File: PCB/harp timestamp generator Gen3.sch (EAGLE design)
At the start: 143 parts, among them IC1 MCP73831T-2ATI/OT, IC10 SN74LVC1G125DBVT, IC11 TLV70033DDCR, IC12 SI8621BC-B-IS, IC13 SI8621BC-B-IS, IC14 SI8621BC-B-IS, IC15 SI8621BC-B-IS, IC16 SI8621BC-B-IS, IC17 SI8621BC-B-IS, IC18 SN74LVC1G125DBVT, IC19 SN74LVC1G125DBVT, IC2 USBLC6-2SC6, IC3 FT232RL, IC4 ICL7673CBAZA-T, IC5 TLV70033DDCR, IC6 ATXMEGA16A4U-AU, IC7 M74VHC1GT126DF1G, IC8 M74VHC1GT126DF1G, IC9 M74VHC1GT126DF1G, Q1 RTU002P02T106, Q2 BC817-40W, Q3 BC817-40LT1SMD, Q4 DMG1012UW, Q5 DMP2035U-7, T1 BC850, T10 BC850, T2 BC850, T3 BC850, T4 BC850, T5 BC850, T6 BC850, T7 BC850, T8 BC850, T9 BC850, X1 B2B-PH-K-S(LF)(SN)

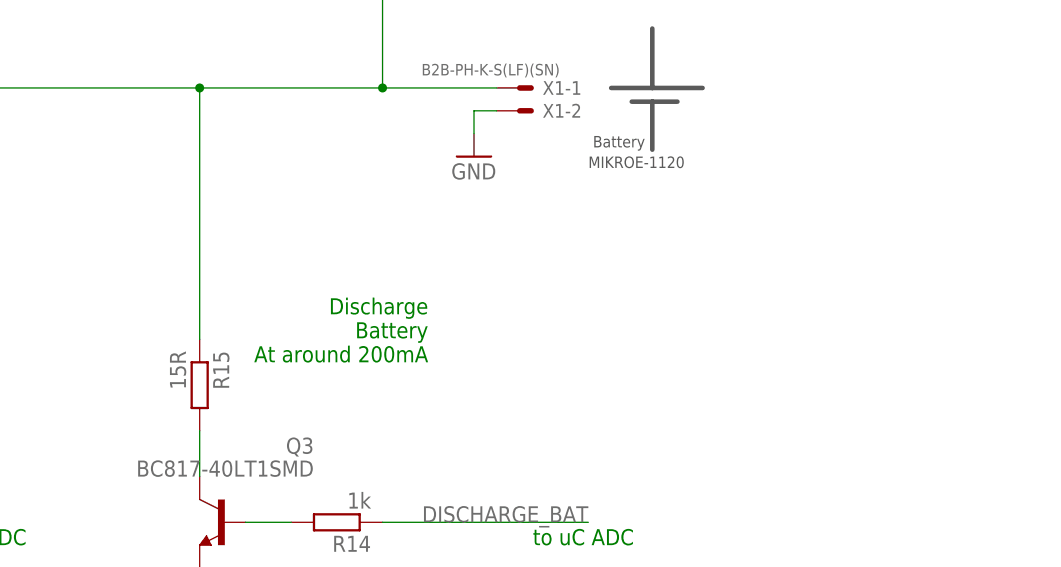
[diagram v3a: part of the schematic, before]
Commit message: Decreased discharge current by ~60 mA to ~175 mA in average.
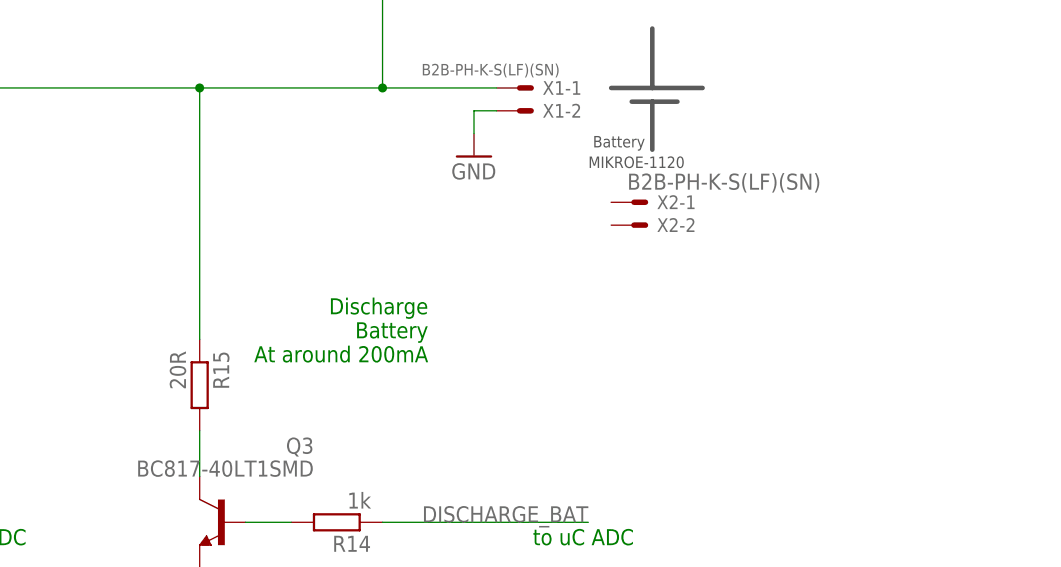
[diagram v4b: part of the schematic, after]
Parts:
- added X2: B2B-PH-K-S(LF)(SN), harp timestamp generator:JST-XH-02-PIN-ROUND-PAD
- R15: value 15R -> 20R
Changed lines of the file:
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@@
 <grid distance="100" unitdist="mil" unit="mil" style="lines" multiple="1" display="no" altdistance="0.01" altunitdist="inch" altunit="inch"/>
 <layers>
-<layer number="1" name="Top" color="4" fill="1" visible="no" active="no"/>
-<layer number="2" name="Route2" color="30" fill="1" visible="no" active="no"/>
-<layer number="3" name="Route3" color="4" fill="3" visible="no" active="no"/>
-<layer number="4" name="Route4" color="1" fill="4" visible="no" active="no"/>
-<layer number="5" name="Route5" color="4" fill="4" visible="no" active="no"/>
-<layer number="6" name="Route6" color="1" fill="8" visible="no" active="no"/>
-<layer number="7" name="Route7" color="4" fill="8" visible="no" active="no"/>
-<layer number="8" name="Route8" color="1" fill="2" visible="no" active="no"/>
-<layer number="9" name="Route9" color="4" fill="2" visible="no" active="no"/>
-<layer number="10" name="Route10" color="1" fill="7" visible="no" active="no"/>
-<layer number="11" name="Route11" color="4" fill="7" visible="no" active="no"/>
-<layer number="12" name="Route12" color="1" fill="5" visible="no" active="no"/>
-<layer number="13" name="Route13" color="4" fill="5" visible="no" active="no"/>
-<layer number="14" name="Route14" color="1" fill="6" visible="no" active="no"/>
-<layer number="15" name="Route15" color="16" fill="1" visible="no" active="no"/>
-<layer number="16" name="Bottom" color="1" fill="1" visible="no" active="no"/>
-<layer number="17" name="Pads" color="2" fill="1" visible="no" active="no"/>
-<layer number="18" name="Vias" color="2" fill="1" visible="no" active="no"/>
-<layer number="19" name="Unrouted" color="6" fill="1" visible="no" active="no"/>
-<layer number="20" name="Dimension" color="15" fill="1" visible="no" active="no"/>
-<layer number="21" name="tPlace" color="7" fill="1" visible="no" active="no"/>
-<layer number="22" name="bPlace" color="7" fill="1" visible="no" active="no"/>
-<layer number="23" name="tOrigins" color="15" fill="1" visible="no" active="no"/>
-<layer number="24" name="bOrigins" color="15" fill="1" visible="no" active="no"/>
-<layer number="25" name="tNames" color="7" fill="1" visible="no" active="no"/>
-<layer number="26" name="bNames" color="7" fill="1" visible="no" active="no"/>
-<layer number="27" name="tValues" color="7" fill="1" visible="no" active="no"/>
-<layer number="28" name="bValues" color="7" fill="1" visible="no" active="no"/>
+<layer number="1" name="Top" color="4" fill="1" visible="yes" active="no"/>
+<layer number="2" name="Route2" color="30" fill="1" visible="yes" active="no"/>
+<layer number="3" name="Route3" color="4" fill="3" visible="yes" active="no"/>
+<layer number="4" name="Route4" color="1" fill="4" visible="yes" active="no"/>
+<layer number="5" name="Route5" color="4" fill="4" visible="yes" active="no"/>
+<layer number="6" name="Route6" color="1" fill="8" visible="yes" active="no"/>
+<layer number="7" name="Route7" color="4" fill="8" visible="yes" active="no"/>
+<layer number="8" name="Route8" color="1" fill="2" visible="yes" active="no"/>
+<layer number="9" name="Route9" color="4" fill="2" visible="yes" active="no"/>
+<layer number="10" name="Route10" color="1" fill="7" visible="yes" active="no"/>
+<layer number="11" name="Route11" color="4" fill="7" visible="yes" active="no"/>
+<layer number="12" name="Route12" color="1" fill="5" visible="yes" active="no"/>
+<layer number="13" name="Route13" color="4" fill="5" visible="yes" active="no"/>
+<layer number="14" name="Route14" color="1" fill="6" visible="yes" active="no"/>
+<layer number="15" name="Route15" color="16" fill="1" visible="yes" active="no"/>
+<layer number="16" name="Bottom" color="1" fill="1" visible="yes" active="no"/>
+<layer number="17" name="Pads" color="2" fill="1" visible="yes" active="no"/>
+<layer number="18" name="Vias" color="2" fill="1" visible="yes" active="no"/>
+<layer number="19" name="Unrouted" color="6" fill="1" visible="yes" active="no"/>
+<layer number="20" name="Dimension" color="15" fill="1" visible="yes" active="no"/>
+<layer number="21" name="tPlace" color="7" fill="1" visible="yes" active="no"/>
+<layer number="22" name="bPlace" color="7" fill="1" visible="yes" active="no"/>
+<layer number="23" name="tOrigins" color="15" fill="1" visible="yes" active="no"/>
+<layer number="24" name="bOrigins" color="15" fill="1" visible="yes" active="no"/>
+<layer number="25" name="tNames" color="7" fill="1" visible="yes" active="no"/>
+<layer number="26" name="bNames" color="7" fill="1" visible="yes" active="no"/>
+<layer number="27" name="tValues" color="7" fill="1" visible="yes" active="no"/>
+<layer number="28" name="bValues" color="7" fill="1" visible="yes" active="no"/>
 <layer number="29" name="tStop" color="7" fill="3" visible="no" active="no"/>
 <layer number="30" name="bStop" color="7" fill="6" visible="no" active="no"/>
@@
 <layer number="35" name="tGlue" color="7" fill="4" visible="no" active="no"/>
 <layer number="36" name="bGlue" color="7" fill="5" visible="no" active="no"/>
-<layer number="37" name="tTest" color="7" fill="1" visible="no" active="no"/>
-<layer number="38" name="bTest" color="7" fill="1" visible="no" active="no"/>
+<layer number="37" name="tTest" color="7" fill="1" visible="yes" active="no"/>
+<layer number="38" name="bTest" color="7" fill="1" visible="yes" active="no"/>
 <layer number="39" name="tKeepout" color="4" fill="11" visible="no" active="no"/>
 <layer number="40" name="bKeepout" color="1" fill="11" visible="no" active="no"/>
@@
 <layer number="44" name="Drills" color="7" fill="1" visible="no" active="no"/>
 <layer number="45" name="Holes" color="7" fill="1" visible="no" active="no"/>
-<layer number="46" name="Milling" color="3" fill="1" visible="no" active="no"/>
-<layer number="47" name="Measures" color="7" fill="1" visible="no" active="no"/>
-<layer number="48" name="Document" color="7" fill="1" visible="no" active="no"/>
-<layer number="49" name="Reference" color="7" fill="1" visible="no" active="no"/>
-<layer number="50" name="dxf" color="7" fill="1" visible="no" active="no"/>
-<layer number="51" name="tDocu" color="7" fill="1" visible="no" active="no"/>
-<layer number="52" name="bDocu" color="7" fill="1" visible="no" active="no"/>
-<layer number="53" name="tGND_GNDA" color="7" fill="9" visible="no" active="no"/>
-<layer number="54" name="bGND_GNDA" color="1" fill="9" visible="no" active="no"/>
-<layer number="56" name="wert" color="7" fill="1" visible="no" active="no"/>
-<layer number="57" name="tCAD" color="7" fill="1" visible="no" active="no"/>
-<layer number="59" name="tCarbon" color="7" fill="1" visible="no" active="no"/>
-<layer number="60" name="bCarbon" color="7" fill="1" visible="no" active="no"/>
+<layer number="46" name="Milling" color="3" fill="1" visible="yes" active="no"/>
+<layer number="47" name="Measures" color="7" fill="1" visible="yes" active="no"/>
+<layer number="48" name="Document" color="7" fill="1" visible="yes" active="no"/>
+<layer number="49" name="Reference" color="7" fill="1" visible="yes" active="no"/>
+<layer number="50" name="dxf" color="7" fill="1" visible="yes" active="no"/>
+<layer number="51" name="tDocu" color="7" fill="1" visible="yes" active="no"/>
+<layer number="52" name="bDocu" color="7" fill="1" visible="yes" active="no"/>
+<layer number="53" name="tGND_GNDA" color="7" fill="9" visible="yes" active="no"/>
+<layer number="54" name="bGND_GNDA" color="1" fill="9" visible="yes" active="no"/>
+<layer number="56" name="wert" color="7" fill="1" visible="yes" active="no"/>
+<layer number="57" name="tCAD" color="7" fill="1" visible="yes" active="no"/>
+<layer number="59" name="tCarbon" color="7" fill="1" visible="yes" active="no"/>
+<layer number="60" name="bCarbon" color="7" fill="1" visible="yes" active="no"/>
 <layer number="88" name="SimResults" color="9" fill="1" visible="no" active="yes"/>
 <layer number="89" name="SimProbes" color="9" fill="1" visible="no" active="yes"/>
@@
 <attribute name="MPN" value="CRCW040210K0FKEDC"/>
 </part>
-<part name="R15" library="rcl" deviceset="R-EU_" device="R2512" value="15R">
+<part name="R15" library="rcl" deviceset="R-EU_" device="R2512" value="20R">
 <attribute name="DIGKEYPN" value="541-2662-1-ND"/>
 <attribute name="MPN" value="RCP2512W25R0GEB"/>
@@
 <part name="GND123" library="supply1" deviceset="GND" device=""/>
 <part name="VDD4" library="supply1" library_urn="urn:adsk.eagle:library:371" deviceset="VDD" device="" value="+3V3_u"/>
+<part name="X2" library="harp timestamp generator" deviceset="JST-XH-02-PIN" device="-ROUND-PAD" value="B2B-PH-K-S(LF)(SN)">
+<attribute name="DIGKEYPN" value="455-1704-ND"/>
+<attribute name="MPN" value="B2B-PH-K-S(LF)(SN)"/>
+</part>
 </parts>
 <sheets>
@@
 <attribute name="VALUE" x="741.68" y="487.68" size="1.778" layer="96" rot="R90"/>
 </instance>
+<instance part="X2" gate="-1" x="353.06" y="434.34" smashed="yes">
+<attribute name="NAME" x="355.6" y="433.578" size="1.524" layer="95"/>
+<attribute name="VALUE" x="352.298" y="435.737" size="1.778" layer="96"/>
+</instance>
+<instance part="X2" gate="-2" x="353.06" y="431.8" smashed="yes">
+<attribute name="NAME" x="355.6" y="431.038" size="1.524" layer="95"/>
+<attribute name="MPN" x="353.06" y="431.8" size="1.778" layer="96" display="off"/>
+<attribute name="DIGKEYPN" x="353.06" y="431.8" size="1.778" layer="96" display="off"/>
+<attribute name="MPN" x="353.06" y="431.8" size="1.778" layer="96" display="off"/>
+<attribute name="DIGKEYPN" x="353.06" y="431.8" size="1.778" layer="96" display="off"/>
+</instance>
 </instances>

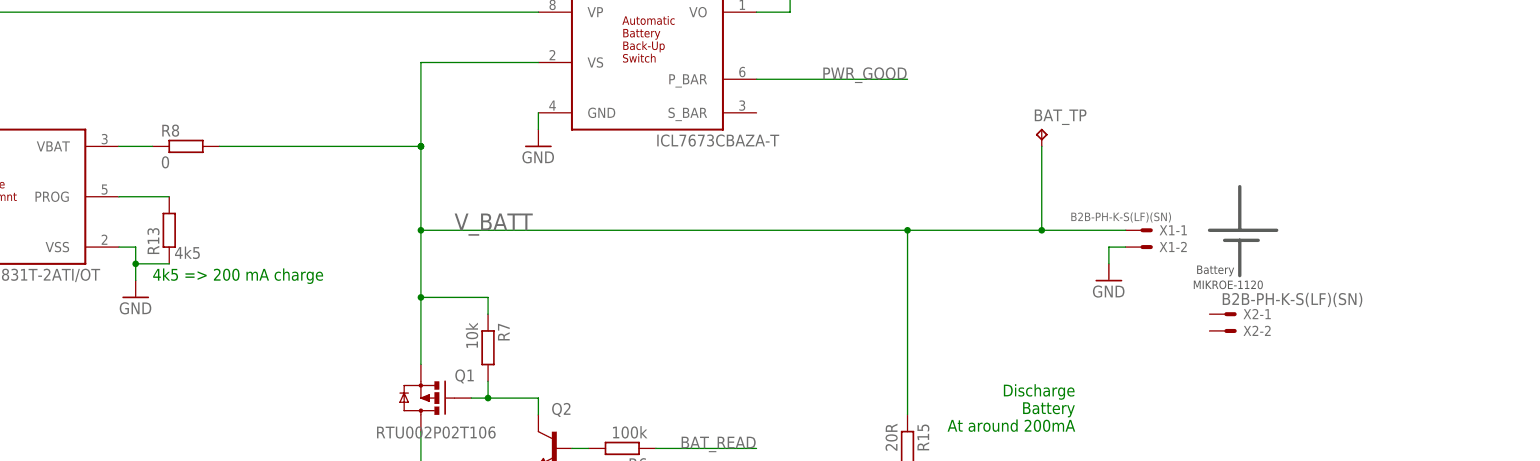
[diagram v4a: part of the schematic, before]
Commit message: Changed battery connection to a new location and added an ON/OFF button.
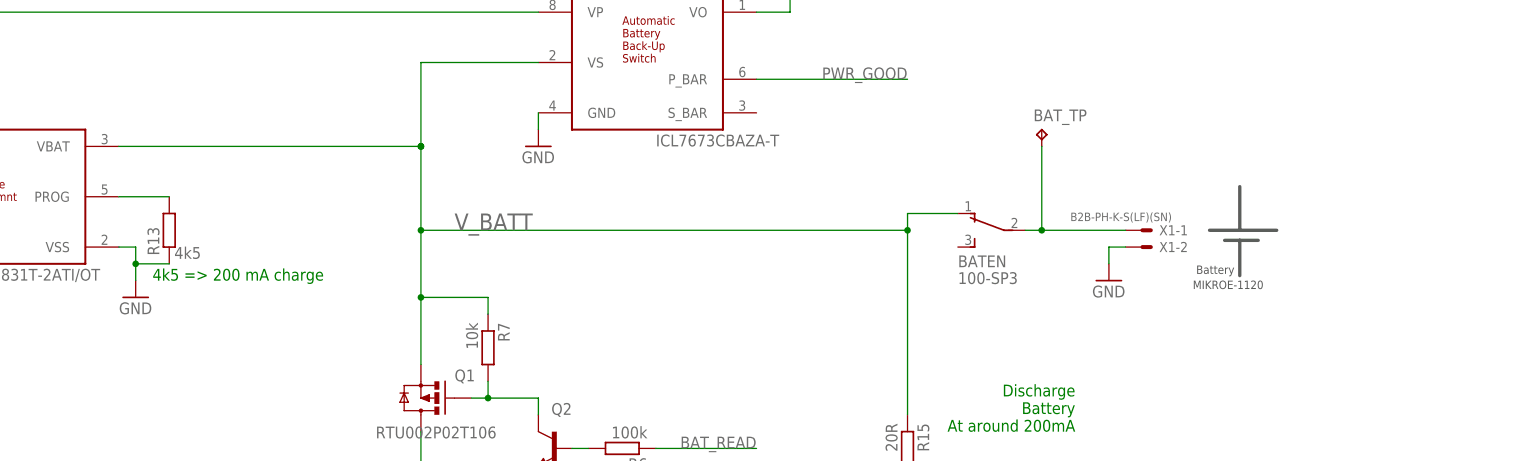
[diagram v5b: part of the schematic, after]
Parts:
- removed R8: 0, rcl:R-EU_R0402
- removed X2: B2B-PH-K-S(LF)(SN), harp timestamp generator:JST-XH-02-PIN-ROUND-PAD
- added BATEN: 100-SP3, cyclops:SPDT_2M-WITHOFF
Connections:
- removed net N$97: IC1.VBAT, R8.1
- new net N$82: BATEN.2, BAT_TP.TP, X1-1.S
- net V_BATT: now also BATEN.1, IC1.VBAT; no longer BAT_TP.TP, R8.2, X1-1.S

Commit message: Added a new power switcher.
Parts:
- added C41, C42: 100nF, rcl:C-EUC0402
- added D1, D2: DNI, harp timestamp generator Gen3:MBRM120
- added R20: 0R, rcl:R-EU_R0402
- added R26: DNI, rcl:R-EU_R0402
- added R_I_MAX: 1k, rcl:R-EU_R0402
- BATEN: DIGIKEY_PN (none) -> CKN1045-ND Mouser: 611-7101-051; MPN (none) -> 7101MD9ABE
- BUTTON: device harp timestamp generator:SPDT_CFPA -> harp timestamp generator Gen3:SPDT_CFPA; DIGIKEY_PN (none) -> 563-1246-1-ND; DIGKEYPN 563-1246-1-ND -> (none)
- C1, C12, C13, C14, C15, C16, C17, C18, C19, C20, C21, C22, C25, C26, C27, C28, C3, C30, C31, C32, C35, C36, C37, C38, C5, C62, C7, C9: DIGIKEY_PN (none) -> 445-6899-2-ND; DIGKEYPN 445-6899-2-ND -> (none)
- C10, C11, C23, C24, C8: DIGIKEY_PN (none) -> 587-2786-1-ND; DIGKEYPN 587-2786-1-ND -> (none)
- C2: DIGIKEY_PN (none) -> 587-2237-1-ND; DIGKEYPN 587-2237-1-ND -> (none)
- C29: DIGIKEY_PN (none) -> 490-3263-1-ND; DIGKEYPN 490-3263-1-ND -> (none)
- C33, C34: value 10n -> 10nF; DIGIKEY_PN (none) -> 1276-1028-1-ND; DIGKEYPN 1276-1028-1-ND -> (none)
- C39: DIGIKEY_PN (none) -> P19702CT-ND; NOTES - -> (none); TYPE TH -> (none)
- C4, C6: DIGIKEY_PN (none) -> 478-1078-1-ND; DIGKEYPN 478-1078-1-ND -> (none)
- C40: DIGIKEY_PN (none) -> 399-11875-1-ND; MPN C0402C331J5GACTU -> C0402C331JAGAC7867; NOTES - -> (none); TYPE SMD -> (none)
- CLKIN, CLKOUT0, CLKOUT1, CLKOUT2, CLKOUT3, CLKOUT4, CLKOUT5: device harp timestamp generator:STEREO_JACK -> harp timestamp generator Gen3:STEREO_JACK; DIGIKEY_PN (none) -> SC1489-1-ND; DIGKEYPN SC1489-1-ND -> (none)
- F1: device harp timestamp generator:BLM15HF0603 -> harp timestamp generator Gen3:BLM15HF0603; DIGIKEY_PN (none) -> 490-3997-1-ND; DIGKEYPN 490-3997-1-ND -> (none)
- IC1: value MCP73831T-2ATI/OT -> MCP73831; device harp timestamp generator:MCP73831T-2ATI/OT -> harp timestamp generator Gen3:MCP73831T-2ATI/OT; DIGIKEY_PN (none) -> MCP73831T-2ATI/OTCT-ND; DIGKEYPN MCP73831T-2ATI/OTCT-ND -> (none)
- IC10, IC18, IC19: DIGIKEY_PN (none) -> 296-26595-1-ND; DIGKEYPN 296-26595-1-ND -> (none)
- IC11, IC5: device harp timestamp generator:TLV700XX -> harp timestamp generator Gen3:TLV700XX; DIGIKEY_PN (none) -> 296-27937-6-ND; DIGKEYPN 296-27937-6-ND -> (none)
- IC12, IC13, IC14, IC15, IC16, IC17: value SI8621BC-B-IS -> SI8621BC; device harp timestamp generator:SI8621BC-B-IS -> harp timestamp generator Gen3:SI8621BC-B-IS; DIGIKEY_PN (none) -> 336-2064-5-ND; DIGKEYPN 336-2064-5-ND -> (none)
- IC2: device harp timestamp generator:USBLC6-2 -> harp timestamp generator Gen3:USBLC6-2; DIGIKEY_PN (none) -> 497-5235-1-ND; DIGKEYPN 497-5235-1-ND -> (none)
- IC3: value FT232RL -> FTDI232; device harp timestamp generator:FT232RL -> harp timestamp generator Gen3:FT232RL; DIGIKEY_PN (none) -> 768-1007-1-ND; DIGKEYPN 768-1007-1-ND -> (none)
- IC4: value ICL7673CBAZA-T -> TPS2114; device harp timestamp generator:ICL7673CBAZA-T -> harp timestamp generator Gen3:TPS2114; DIGIKEY_PN (none) -> 296-16939-1-ND; DIGKEYPN ICL7673CBAZA-TCT-ND -> (none); MPN ICL7673CBAZA-T -> TPS2114APWR
- IC6: device harp timestamp generator:AT-XMEGA-XXA4-AU -> harp timestamp generator Gen3:AT-XMEGA-XXA4-AU; DIGIKEY_PN (none) -> ATXMEGA16A4U-AU-ND; DIGKEYPN ATXMEGA16A4U-AU-ND -> (none)
- IC7, IC8, IC9: DIGIKEY_PN (none) -> M74VHC1GT126DF1GOSCT-ND; DIGKEYPN M74VHC1GT126DF1GOSCT-ND -> (none)
- L1: DIGIKEY_PN (none) -> 240-2389-1-ND; DIGKEYPN 240-2389-1-ND -> (none)
- LED1, LED2, LED3, LED4, LED5: value 569-0112-100 -> LED-2HI; device harp timestamp generator:LED_2X_VERTICAL -> harp timestamp generator Gen3:LED_2X_VERTICAL; DIGIKEY_PN (none) -> 350-1782-ND; DIGKEYPN 350-1782-ND -> (none); MPN 5690-111-100F -> 5690111100F
- OSC1: value OSCILLATOR -> OSC 32MHZ; device harp timestamp generator:OSCILLATOR -> harp timestamp generator Gen3:OSCILLATOR; DIGIKEY_PN (none) -> 1908-1044-1-ND; DIGKEYPN 1908-1044-1-ND -> (none)
- PDI: DIGIKEY_PN (none) -> 609-3210-ND; DIGKEYPN 609-3210-ND -> (none)
- Q1: device harp timestamp generator:MOSFET-PCHANNEL-ROHM -> harp timestamp generator Gen3:MOSFET-PCHANNEL-ROHM; DIGIKEY_PN (none) -> RTU002P02T106CT-ND; DIGKEYPN RTU002P02T106CT-ND -> (none)
- Q2: DIGIKEY_PN (none) -> 1727-6185-1-ND; DIGKEYPN 1727-6185-1-ND -> (none)
- Q3: value BC817-40LT1SMD -> SBC817; device transistor-npn:BC817-40LT1SMD -> harp timestamp generator Gen3:BC817-40LT1SMD; DIGIKEY_PN (none) -> SBC817-40LT1GOSCT-ND; DIGKEYPN SBC817-40LT1GOSCT-ND -> (none)
- Q4: device harp timestamp generator:DMG1012UW -> harp timestamp generator Gen3:DMG1012UW; DIGIKEY_PN (none) -> DMG1012UW-7DICT-ND; DIGKEYPN DMG1012UW-7DICT-ND -> (none)
- Q5: device harp timestamp generator:DMP2035U-7 -> harp timestamp generator Gen3:DMP2035U-7; DIGIKEY_PN (none) -> DMP2035U-7DICT-ND; DIGKEYPN DMP2035U-7DICT-ND -> (none)
- R1: DIGIKEY_PN (none) -> 541-3965-1-ND; DIGKEYPN 541-3965-1-ND -> (none)
- R10, R11, R12: DIGIKEY_PN (none) -> 311-100DCT-ND; DIGKEYPN 311-100DCT-ND -> (none)
- R13, R17, R19: DIGIKEY_PN (none) -> YAG1444CT-ND; DIGKEYPN YAG1444CT-ND -> (none)
- R14: DIGIKEY_PN (none) -> RMCF0402FT1K00CT-ND; DIGKEYPN 541-3959-1-ND -> (none); MPN CRCW040210K0FKEDC -> RMCF0402FT1K00
- R15: DIGIKEY_PN (none) -> 541-2662-1-ND; DIGKEYPN 541-2662-1-ND -> (none)
- R16, R18, R3, R7, R9: DIGIKEY_PN (none) -> RMCF0402FT10K0CT-ND; DIGKEYPN 541-3959-1-ND -> (none); MPN CRCW040210K0FKEDC -> RMCF0402FT10K0
- R2: DIGIKEY_PN (none) -> 541-10.0YCT-ND; DIGKEYPN 541-10.0YCT-ND -> (none)
- R21, R22, R23, R24, R25, R27, R28, R29, R30, R31: DIGIKEY_PN (none) -> RMCF0402FT1K00CT-ND; DIGKEYPN 541-1.00KYCT-ND -> (none); MPN CRCW04021K00FKEDHP -> RMCF0402FT1K00
- R33, R34, R35, R36, R37, R40, R41, R42, R44, R45: DIGIKEY_PN (none) -> 311-330LRCT-ND; DIGKEYPN 311-330LRCT-ND -> (none)
- R4: DIGIKEY_PN (none) -> P51KDCCT-ND; DIGKEYPN P51KDCCT-ND -> (none)
- R48: DIGIKEY_PN (none) -> P15984CT-ND; DIGKEYPN P15984CT-ND -> (none)
- R5: value 15K 0.1% => 14k7 -> 14k7; DIGIKEY_PN (none) -> YAG4174CT-ND; DIGKEYPN YAG4174CT-ND -> (none)
- R50: DIGIKEY_PN (none) -> RMCF0402FT10K0CT-ND; MPN CRCW040210K0FKED -> RMCF0402FT10K0; NOTES - -> (none); TYPE SMD -> (none)
- R54, R55: DIGIKEY_PN (none) -> RMCF0402FT10K0CT-ND; DIGKEYPN 541-1.00KYCT-ND -> (none); MPN CRCW04021K00FKEDHP -> RMCF0402FT10K0
- R6: value 100k -> 14k7; DIGIKEY_PN (none) -> YAG4174CT-ND; DIGKEYPN P15984CT-ND -> (none); MPN ERJ-2RHD1002X -> RT0402BRD0714K7L
- SV1: device harp timestamp generator:ML10L -> harp timestamp generator Gen3:ML10L; DIGIKEY_PN (none) -> S9177-ND; DIGKEYPN S9177-ND -> (none)
- T1, T10, T2, T3, T4, T5, T6, T7, T8, T9: device transistor:BC850 -> harp timestamp generator Gen3:BC850; DIGIKEY_PN (none) -> 1727-4862-1-ND; DIGKEYPN 1727-4862-1-ND -> (none)
- USB: device harp timestamp generator:USB_MINI_B -> harp timestamp generator Gen3:USB_MINI_B; DIGIKEY_PN (none) -> H2960TR-ND; DIGKEYPN H2960TR-ND -> (none)
- X1: device harp timestamp generator:JST-XH-02-PIN-ROUND-PAD -> harp timestamp generator Gen3:JST-XH-02-PIN-ROUND-PAD; DIGIKEY_PN (none) -> 455-1704-ND; DIGKEYPN 455-1704-ND -> (none)
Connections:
- new net N$114: IC4.ILIM, R_I_MAX.1
- new net N$139: D1.C, D2.C, IC4.D0
- new net N$140: IC4.D1, R20.2
- net +5V: now also IC4.OUT, R26.1; no longer IC4.VO
- net +5_USB: now also C42.1, D1.A, IC4.IN1; no longer IC4.VP
- net GND: now also C41.2, C42.2, R20.1, R_I_MAX.2
- net PWR_GOOD: now also IC4.STAT, R26.2; no longer IC4.P_BAR
- net V_BATT: now also C41.1, D2.A, IC4.IN2; no longer IC4.VS
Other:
- note removed: "DigiKey: 1908-1044-1-ND"
- moved on the sheet: +3V3_TP, +5V_TP, BATEN, BAT_TP, BUTTON, C1, C10, C11, C12, C13, C14, C15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
